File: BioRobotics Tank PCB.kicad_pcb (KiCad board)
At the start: 2 copper layers, 72 x 90 mm, 72 parts, among them J1 Conn_01x02, J2 Conn_01x02, J3 Conn_01x02, J4 Conn_01x02, J5 Conn_01x02, J6 Conn_01x02, J7 Conn_01x02, J8 Conn_02x05_Odd_Even, J9 Conn_01x05, Q1 PSMN4R5-30YLC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

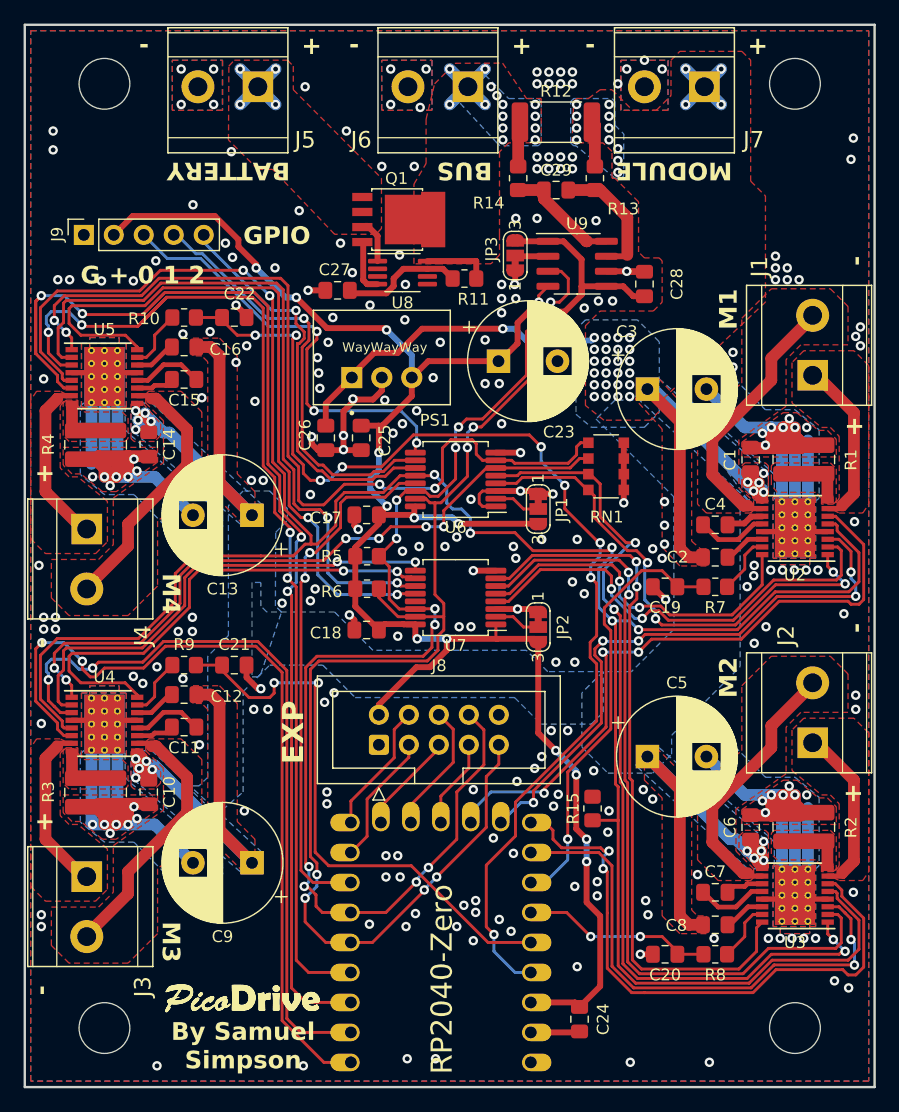
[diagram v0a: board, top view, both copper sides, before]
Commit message: Move some via's to improve routing / ground width
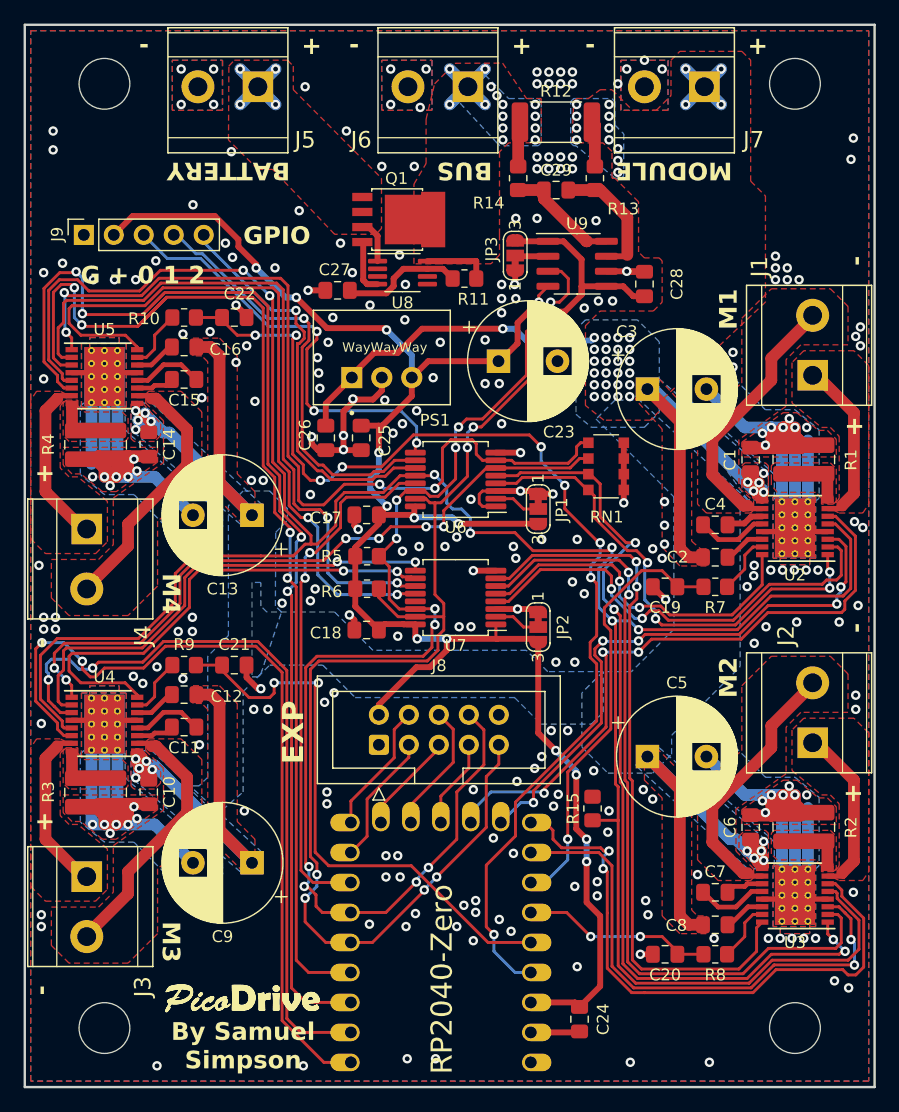
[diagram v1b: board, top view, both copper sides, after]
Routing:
- net /M4_PH: track 91.2 -> 94.9 mm
- net /M4_EN: track 103.5 -> 101.5 mm
- net /~{M1_FAULT}: track 43.2 -> 41.6 mm
- net /M1_EN: track 54.9 -> 53.7 mm
- net /M1_PH: track 49.5 -> 48.2 mm
- net GND1: vias 260 -> 264

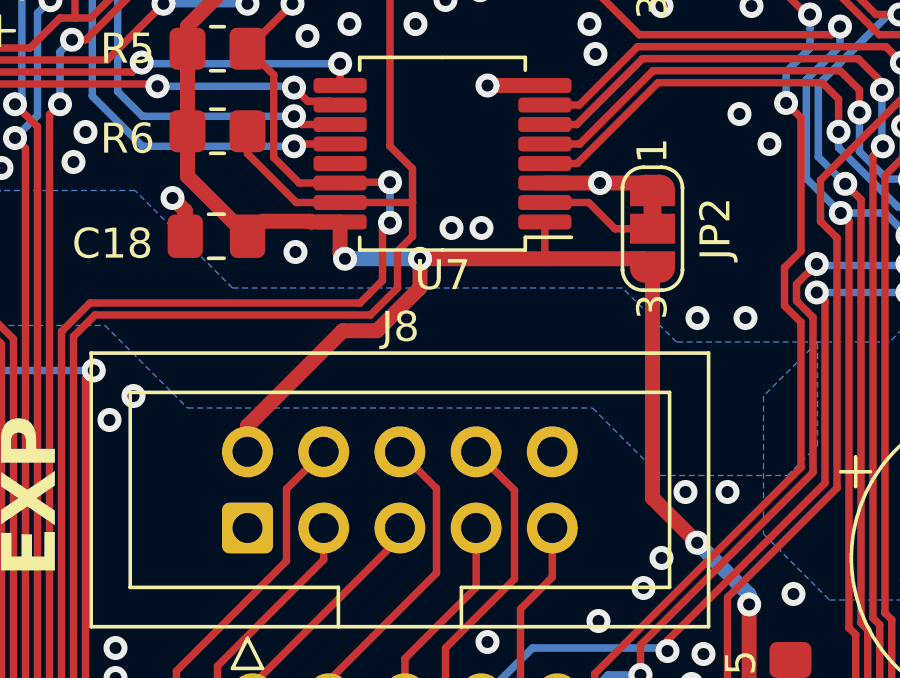
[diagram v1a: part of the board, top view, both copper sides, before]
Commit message: Improve ground connection over Vdrive trace
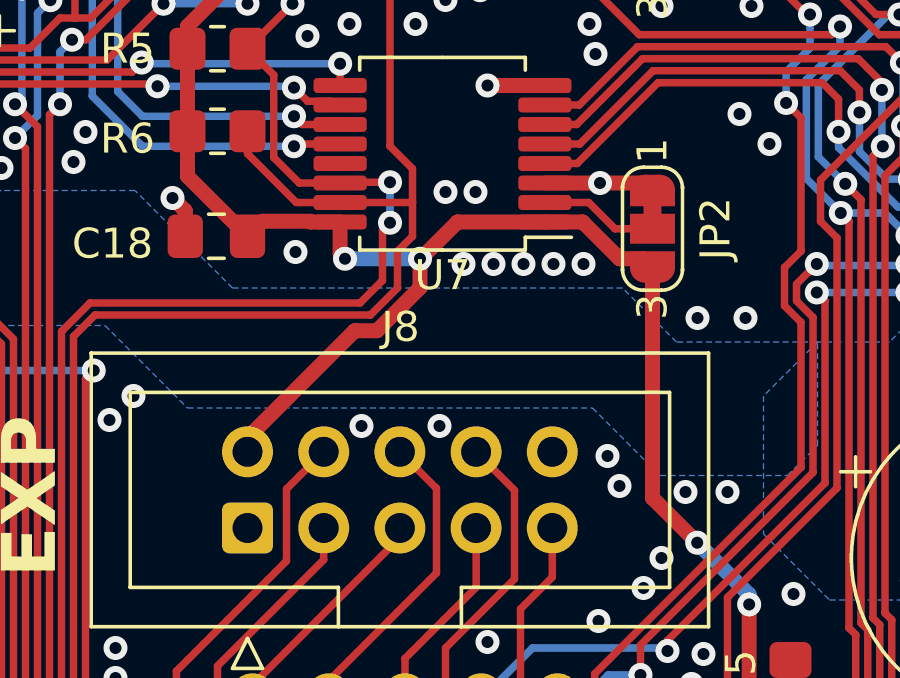
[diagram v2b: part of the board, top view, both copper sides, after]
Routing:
- net GND1: vias 264 -> 273
